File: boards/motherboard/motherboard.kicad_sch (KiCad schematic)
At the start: 49 parts, among them CN1 HY931147C, J1 Adaptor, J2 Boot Selection, J3 Arduino Connector, J4 Arduino Connector, J5 Arduino Connector, J6 Arduino Connector, J7 JTAG, SW1 Reset, U1 STM32F407VETx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

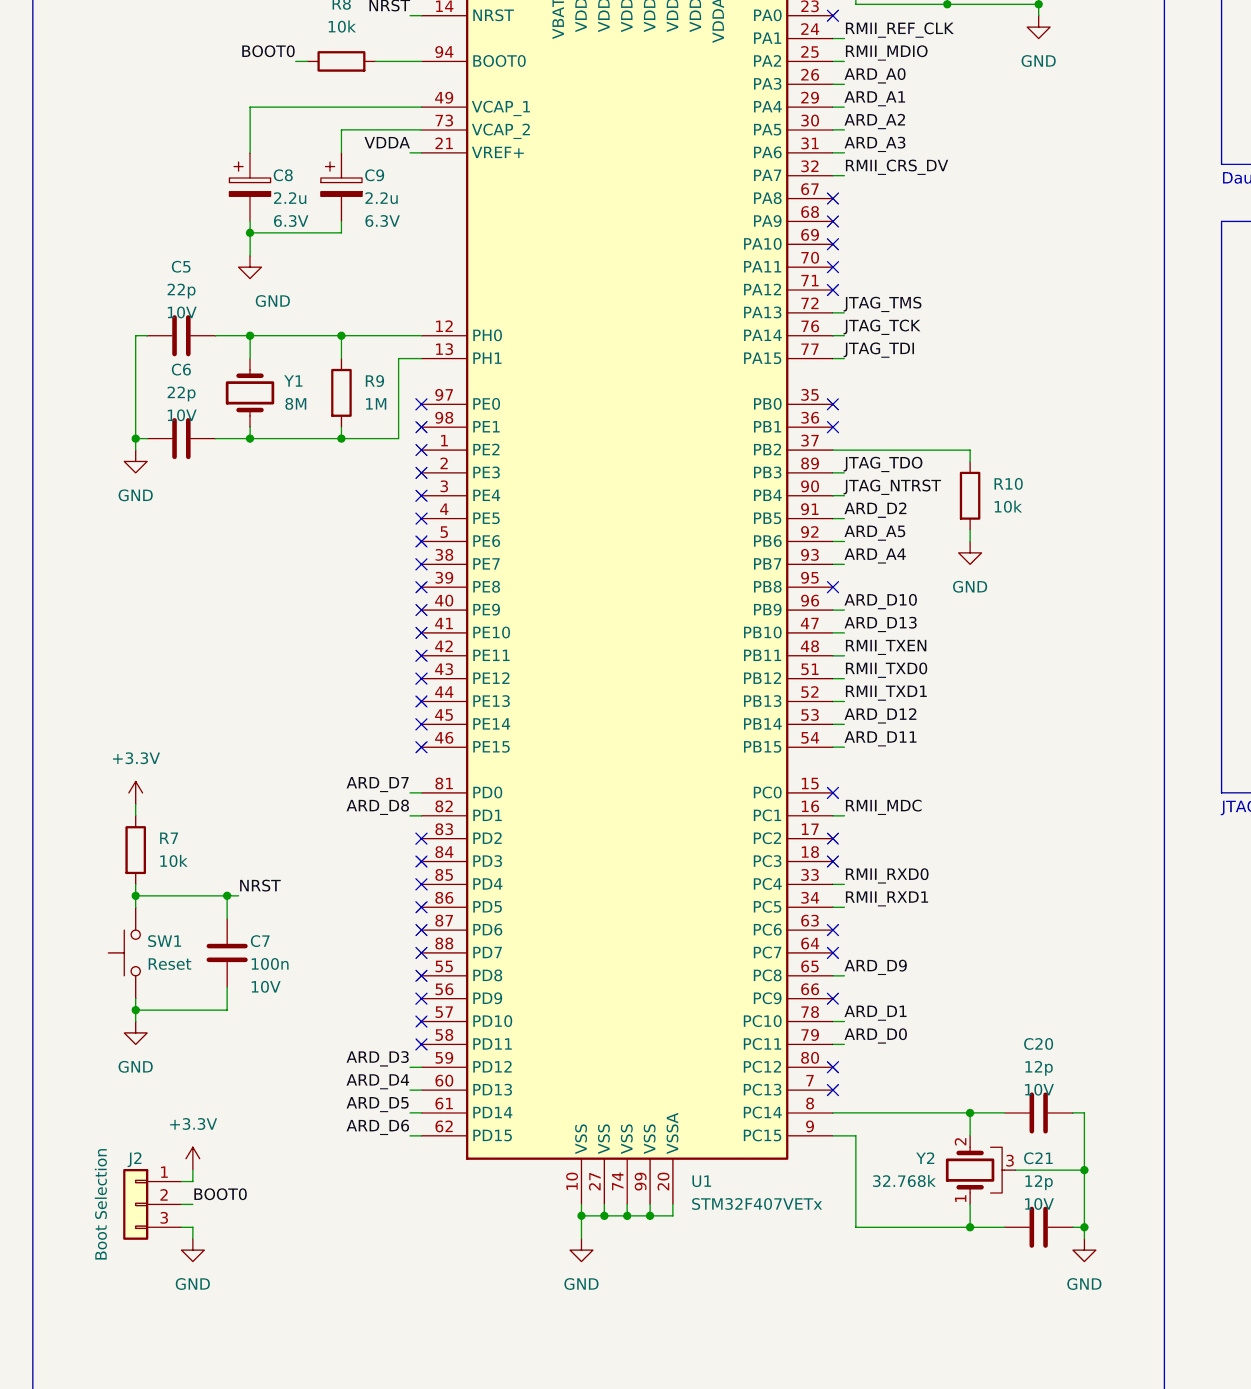
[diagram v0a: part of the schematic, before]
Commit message: feat: assign footprints
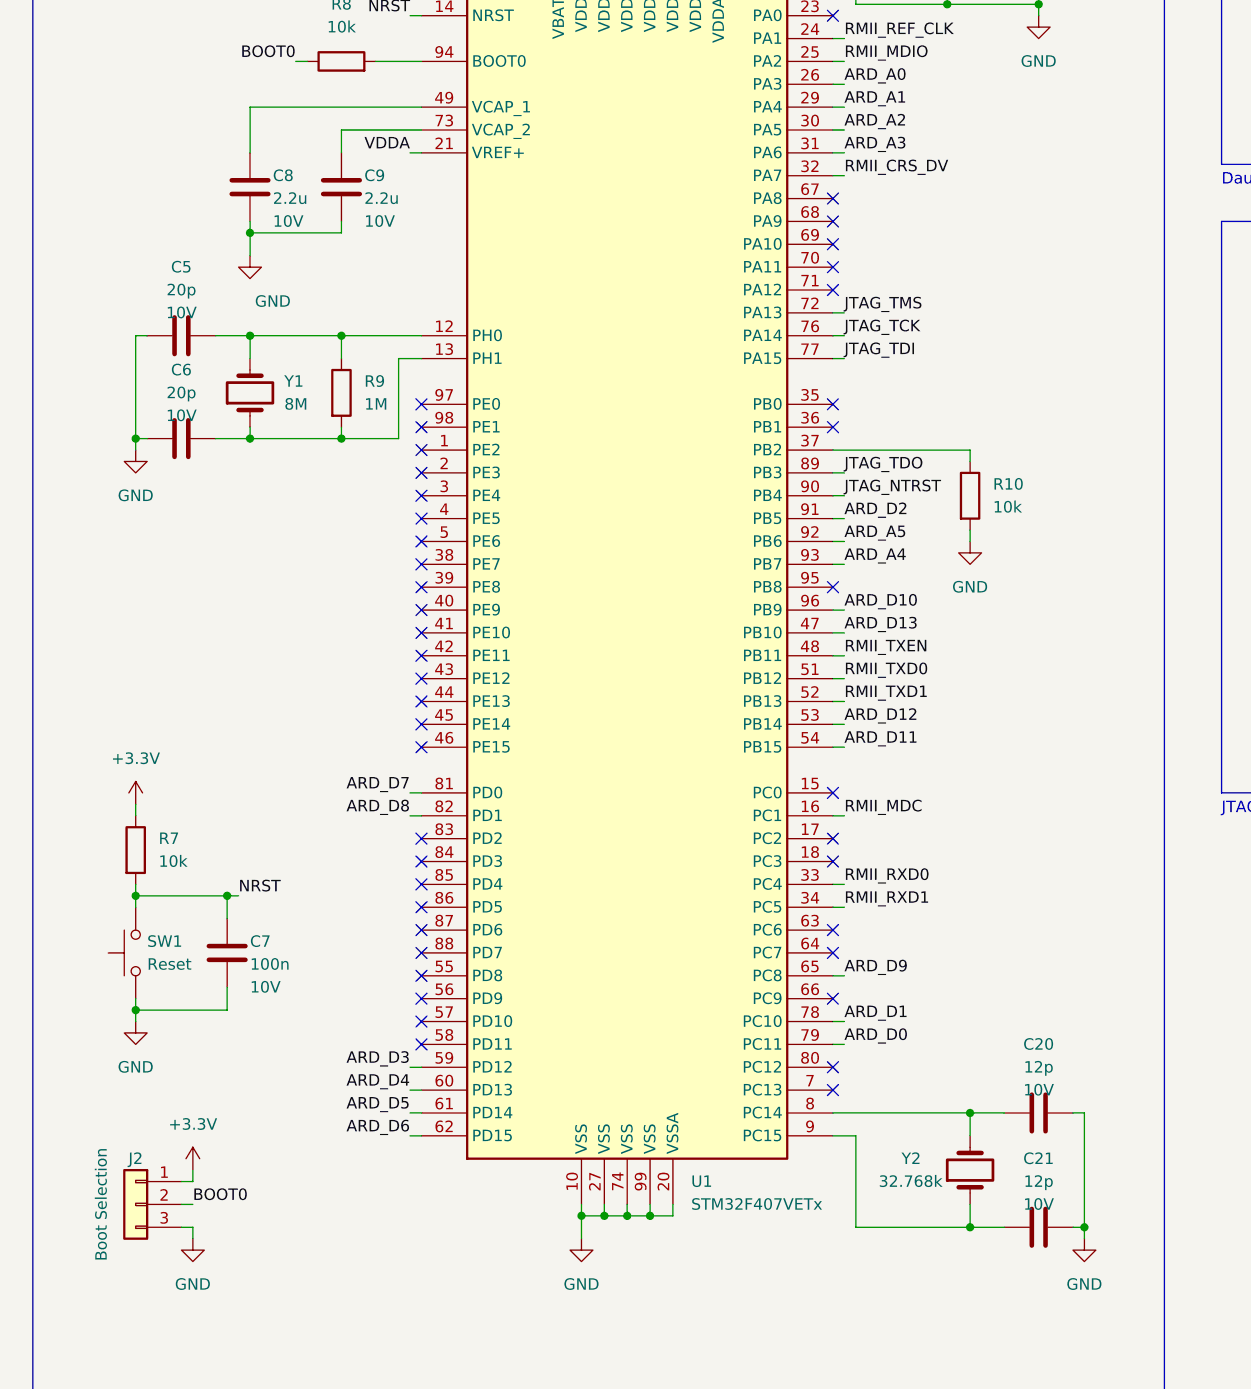
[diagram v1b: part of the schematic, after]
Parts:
- removed C8, C9: 2.2u, symbol Device:C_Polarized
- removed Y2: 32.768k, symbol Device:Crystal_GND3
- added C8, C9: 2.2u, Capacitor_SMD:C_0603_1608Metric, symbol Device:C
- added Y2: 32.768k, Crystal:Crystal_SMD_3215-2Pin_3.2x1.5mm, symbol Device:Crystal
- C1, C10, C11, C12, C13, C14, C15, C16, C17, C19, C2, C20, C21, C3, C4, C7: footprint (none) -> Capacitor_SMD:C_0603_1608Metric
- C18: footprint (none) -> Capacitor_SMD:CP_Elec_4x5.4
- C5, C6: value 22p -> 20p; footprint (none) -> Capacitor_SMD:C_0603_1608Metric
- CN1: footprint HY931147C:HY931147C -> footprints:HY931147C
- J1: footprint (none) -> Connector_BarrelJack:BarrelJack_Horizontal
- J2: footprint (none) -> Connector_PinHeader_2.54mm:PinHeader_1x03_P2.54mm_Vertical
- J3, J6: footprint (none) -> Connector_PinSocket_2.54mm:PinSocket_1x08_P2.54mm_Vertical
- J4: footprint (none) -> Connector_PinSocket_2.54mm:PinSocket_1x06_P2.54mm_Vertical
- J5: footprint (none) -> Connector_PinSocket_2.54mm:PinSocket_1x10_P2.54mm_Vertical
- J7: footprint (none) -> Connector_PinSocket_2.54mm:PinSocket_2x10_P2.54mm_Vertical
- L1: footprint (none) -> Inductor_SMD:L_0805_2012Metric
- R1, R10, R11, R12, R13, R14, R15, R2, R3, R4, R5, R6, R7, R8, R9: footprint (none) -> Resistor_SMD:R_0603_1608Metric
- SW1: footprint (none) -> footprints:SW_Push_1P1T_NO_5.2x5.2mm
- Y1: footprint (none) -> Crystal:Crystal_SMD_5032-2Pin_5.0x3.2mm
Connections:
- net GND: now also C8.2, C9.2
- net at C21.1, U1.9 (PC15): now also Y2.1
- net at C20.1, U1.8 (PC14): now also Y2.2
- net at U1.49 (VCAP_1): now also C8.1
- net at U1.73 (VCAP_2): now also C9.1

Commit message: feat: first revision of pcb layout
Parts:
- removed CN1: HY931147C, footprints:HY931147C, symbol HY931147C:HY931147C
- added H1, H2, H3, H4: MountingHole, MountingHole:MountingHole_3.2mm_M3, symbol Mechanical:MountingHole
- added U7: HY931147C, HY931147C:HY931147C, symbol HY931147C:HY931147C
- SW1: footprint footprints:SW_Push_1P1T_NO_5.2x5.2mm -> Button_Switch_THT:SW_PUSH_6mm
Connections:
- net +3.3V: now also U7.P$3 (RXCT), U7.P$4 (TXCT)
- net ETH_RX+: now also U7.P$1 (RX+)
- net ETH_RX-: now also U7.P$2 (RX-)
- net ETH_TX+: now also U7.P$5 (TX+)
- net ETH_TX-: now also U7.P$6 (TX-)
- net GND: now also U7.GND1, U7.GND2
- net LED_ACT: now also U7.P$12 (Y-)
- net LED_LINK: now also U7.P$14 (G-)
- net VDD_POE: now also U7.P$9 (V+)
- net VSS_POE: now also U7.P$10 (V-)
- net at R2.2: now also U7.P$11 (Y+)
- net at R3.2: now also U7.P$13 (G+)
